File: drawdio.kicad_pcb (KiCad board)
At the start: 2 copper layers, 45.7 x 12.7 mm, 12 parts, among them P1 CONN_2, P2 CONN_01X01, Q1 BC558, Q2 BC547, U1 LM555N

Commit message: Heavy work
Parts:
- added P3: CONN_01X01, Mounting_Holes:MountingHole_2-5mm, F.Cu at (120.4, 94.0)
- added P4: CONN_01X02, drawdio:RS_mini_speaker_724-3100, F.Cu at (72.1, 86.4)
- added P5: CONN_01X01, Mounting_Holes:MountingHole_2-5mm, F.Cu at (120.4, 78.7)
- added P6: CONN_01X01, Mounting_Holes:MountingHole_2-5mm, F.Cu at (60.7, 94.0)
- added P7: CONN_01X01, Mounting_Holes:MountingHole_2-5mm, F.Cu at (60.7, 78.7)
- added Q3: BC558, Housings_TO-92:TO-92_Molded_Wide_Oval, F.Cu at (90.2, 91.4)
- added Q4: BC547, Housings_TO-92:TO-92_Molded_Wide_Oval, F.Cu at (99.1, 91.4)
- BT1: footprint Pin_Headers:Pin_Header_Straight_1x02 -> drawdio:CR2025_Keystone_3002_button_cell_holder_SMT
- P1: value CONN_2 -> CONN_01X01; footprint Pin_Headers:Pin_Header_Straight_1x02 -> drawdio:Drawdio_conn
- P2: footprint Pin_Headers:Pin_Header_Straight_1x01 -> drawdio:Drawdio_conn
- Q1, Q2: footprint drawdio:TO-92_JorFru_compact -> Housings_TO-92:TO-92_Molded_Wide_Oval
- moved P1 66.8 mm to (57.7, 86.4), turned to 270 degrees
- moved P2 57.2 mm to (146.1, 86.4), turned to 90 degrees
- moved BT1 38.1 mm to (130.8, 86.4), turned to 0 degrees
- moved C3 12.8 mm to (108.0, 78.7), turned to 180 degrees
- moved Q2 11.8 mm to (85.1, 87.6)
- moved C4 10.2 mm to (88.9, 80.0), turned to 180 degrees
- moved C2 10.1 mm to (106.7, 94.0), turned to 180 degrees
- moved C1 5.71 mm to (97.8, 80.0), turned to 180 degrees
- moved R1 4.60 mm to (116.8, 86.4)
- moved R2 4.60 mm to (114.3, 86.4)
- moved Q1 4.58 mm to (94.0, 87.6), turned to 0 degrees
- moved U1 0.80 mm to (102.9, 82.5)
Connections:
- P2 pad 1: Net-(C4-Pad2) -> Net-(P2-Pad1)
- Q1 pad 1: VCC -> Net-(P4-Pad2)
- Q1 pad 3: Net-(C4-Pad1) -> VCC
- Q2 pad 1: Net-(C4-Pad1) -> Net-(P4-Pad2)
- R2 pad 1: Net-(P1-Pad2) -> Net-(P2-Pad1)
- U1 pad 7: Net-(P1-Pad2) -> Net-(P2-Pad1)
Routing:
- net Net-(P1-Pad1): track 4.23 -> 66.7 mm
- net VCC: track 54.7 -> 0.00 mm
- net Net-(P2-Pad1): track 0.00 -> 50.9 mm
- net Net-(P4-Pad2): track 0.00 -> 40.2 mm
- net Net-(P1-Pad2): track 21.9 -> 0.00 mm
- net Net-(C4-Pad1): track 13.0 -> 24.1 mm
- net Net-(C4-Pad2): track 6.34 -> 15.8 mm
- net Net-(Q1-Pad2): track 13.3 -> 16.8 mm
- net Net-(C3-Pad1): track 23.6 -> 26.0 mm
- added copper zone on B.Cu, net VCC
- removed copper zone on B.Cu, net GND
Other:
- board size 45.7 x 12.7 mm -> 95.5 x 20.3 mm

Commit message: Added holes
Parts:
- added P8: CONN_01X01, drawdio:Symbol_OSHW-Logo_SilkScreen_BIG, B.Cu at (150.1, 86.1)

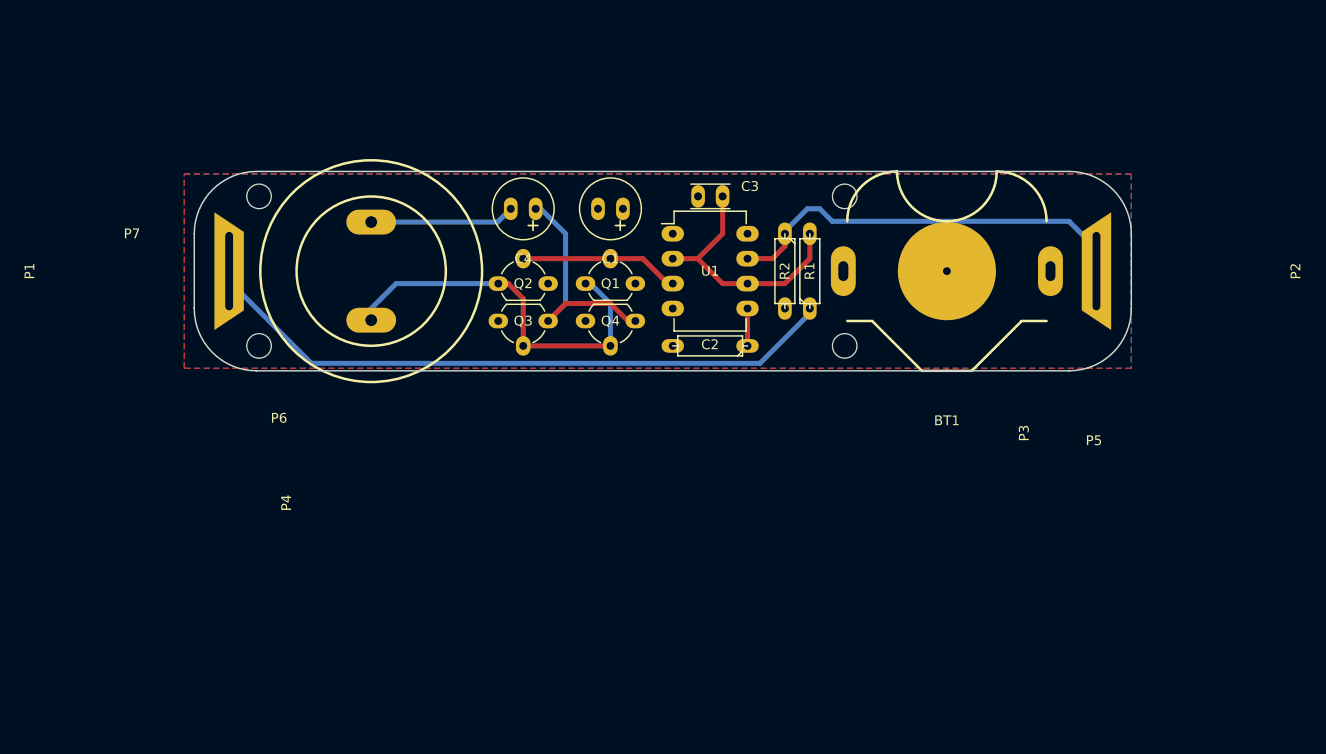
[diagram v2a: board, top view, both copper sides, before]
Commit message: Añadidas resistencias
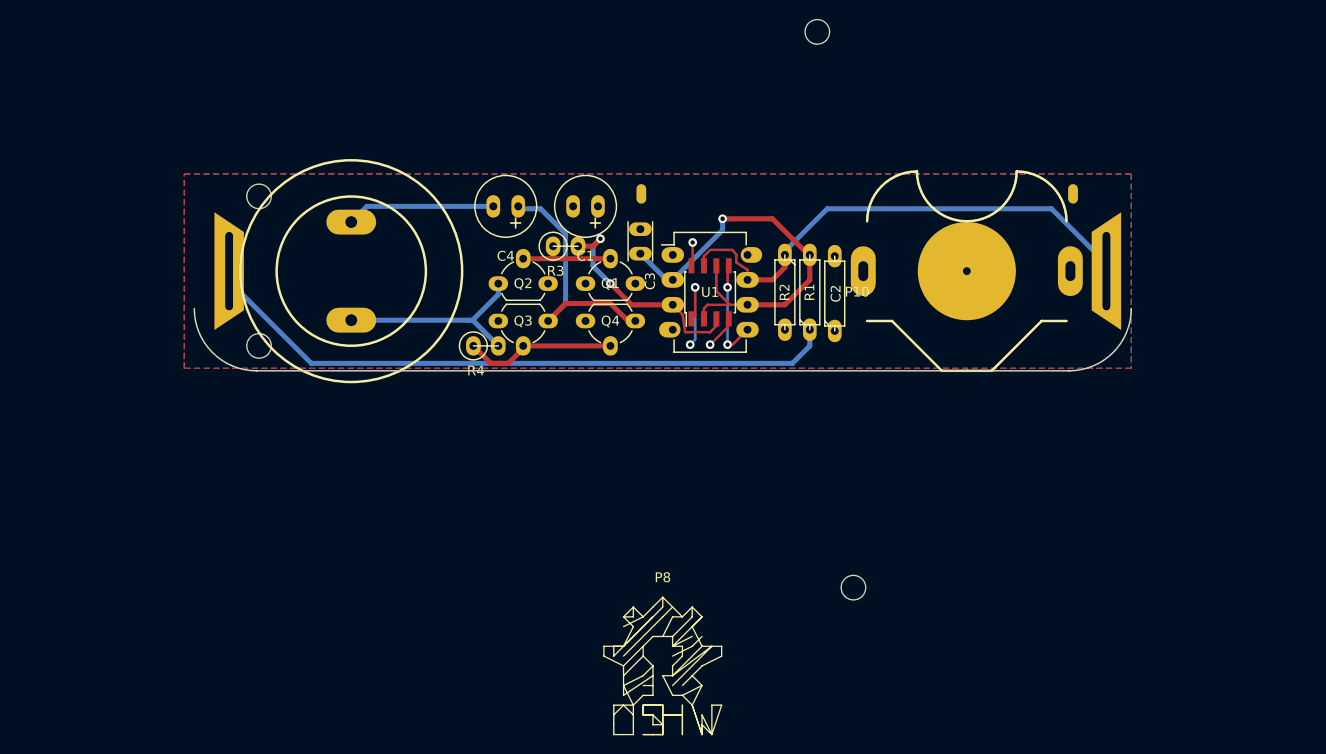
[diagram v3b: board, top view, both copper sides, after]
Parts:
- added P10: CONN_01X02, drawdio:AAA_cell_holder, F.Cu at (121.7, 78.5)
- added P9: CONN_02X04, Housings_SOIC:SOIC-8_3.9x4.9mm_Pitch1.27mm, F.Cu at (106.7, 88.5)
- added R3: R, Discret:R1, F.Cu at (91.9, 83.8)
- added R4: R, Discret:R1, F.Cu at (83.8, 94.0)
- P8: moved to F.Cu
- moved P8 52.4 mm to (101.9, 106.6), turned to 0 degrees
- moved P3 24.7 mm to (121.3, 118.6)
- moved P5 17.0 mm to (117.6, 62.0)
- moved C2 13.8 mm to (119.4, 88.6), turned to 90 degrees
- moved C3 10.2 mm to (99.6, 84.6), turned to 90 degrees
- moved C1 2.55 mm to (95.2, 79.8)
- moved R1 2.16 mm to (116.8, 88.5)
- moved R2 2.16 mm to (114.3, 88.5)
- moved U1 2.16 mm to (102.9, 84.7)
- moved BT1 2.03 mm to (132.8, 86.4)
- moved P4 2.03 mm to (70.1, 86.4)
- moved C4 1.80 mm to (87.1, 79.8)
- moved P2 1.02 mm to (147.1, 86.4)
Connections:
- net Net-(C2-Pad1) renamed /pin5
- net Net-(C3-Pad1) renamed /pin2
- net Net-(P2-Pad1) renamed /pin7
- P3 pad 1: (no net) -> Net-(P3-Pad1)
- P5 pad 1: (no net) -> Net-(P5-Pad1)
- P6 pad 1: (no net) -> Net-(P6-Pad1)
- P7 pad 1: (no net) -> Net-(P7-Pad1)
- Q3 pad 2: Net-(P4-Pad2) -> Net-(Q3-Pad2)
- Q4 pad 2: Net-(P4-Pad2) -> Net-(Q3-Pad2)
- U1 pad 3: Net-(Q1-Pad2) -> /pin3
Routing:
- net /pin3: track 0.00 -> 23.9 mm, vias 0 -> 2
- net Net-(P4-Pad2): track 40.2 -> 21.6 mm
- net /pin2: track 26.0 -> 43.3 mm, vias 0 -> 1
- net Net-(Q3-Pad2): track 0.00 -> 15.6 mm
- net GND: track 0.00 -> 9.42 mm, vias 0 -> 2
- net /pin5: track 3.81 -> 10.7 mm, vias 0 -> 2
- net Net-(Q1-Pad2): track 16.8 -> 10.2 mm
- net VCC: track 0.00 -> 5.86 mm, vias 0 -> 2
- net /pin7: track 50.9 -> 54.6 mm
- net Net-(C4-Pad1): track 24.1 -> 26.0 mm
- net Net-(C4-Pad2): track 15.8 -> 15.1 mm
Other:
- board size 95.5 x 20.3 mm -> 95.5 x 6.3 mm
- net class micro added: clearance 0.254, trace_width 0.254, via_dia 0.889, via_drill 0.635

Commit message: AAA cell added
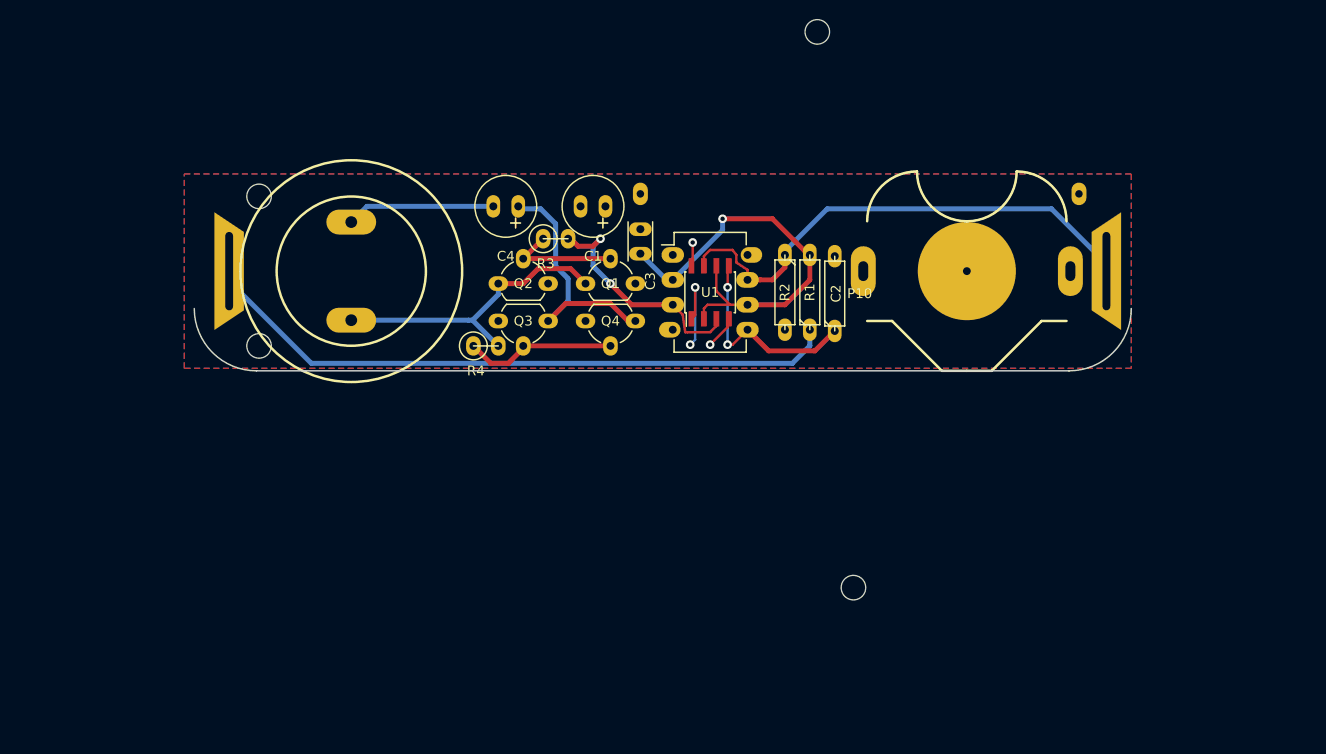
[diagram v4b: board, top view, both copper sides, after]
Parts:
- removed P8: CONN_01X01, drawdio:Symbol_OSHW-Logo_SilkScreen_BIG
- moved R3 1.27 mm to (90.9, 83.1)
- moved C1 0.76 mm to (96.0, 79.8)
- moved P10 0.25 mm to (121.9, 78.5)
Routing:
- net /pin5: track 10.7 -> 21.4 mm
- net Net-(P4-Pad2): track 21.6 -> 31.2 mm
- net Net-(Q1-Pad2): track 10.2 -> 11.8 mm
- net /pin3: track 23.9 -> 25.2 mm

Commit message: Pre-release 1.0
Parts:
- moved P3 23.6 mm to (121.9, 95.0)
- moved P5 16.3 mm to (121.9, 77.7)
- moved P4 2.54 mm to (72.6, 86.4)
- moved P1 2.54 mm to (60.2, 86.4)
- moved P6 1.52 mm to (62.2, 94.0)
- moved P7 1.52 mm to (62.2, 78.7)
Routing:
- net Net-(P1-Pad1): track 67.0 -> 63.4 mm
- net Net-(P4-Pad2): track 31.2 -> 28.7 mm
- net Net-(C4-Pad2): track 15.1 -> 12.6 mm
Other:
- board size 95.5 x 6.3 mm -> 94 x 22 mm

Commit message: Reviewed and ready
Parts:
- added G***: LOGO, uc3music_logos:logo_guitar_22.5x7.7mm_mirror, B.Cu at (135.6, 93.0)
- added G***: LOGO, uc3music_logos:logo_pick_15x15mm, B.Cu at (134.6, 83.3)
- added G***: LOGO, uc3music_logos:logo_text_20x3.5mm, B.Cu at (73.2, 86.4)
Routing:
- net Net-(P1-Pad1): track 63.4 -> 64.1 mm
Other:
- board text added: "Drawdio"
- board text added: "V1.0"
